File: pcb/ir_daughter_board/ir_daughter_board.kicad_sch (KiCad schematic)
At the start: 5 parts, among them J1 USB_OTG

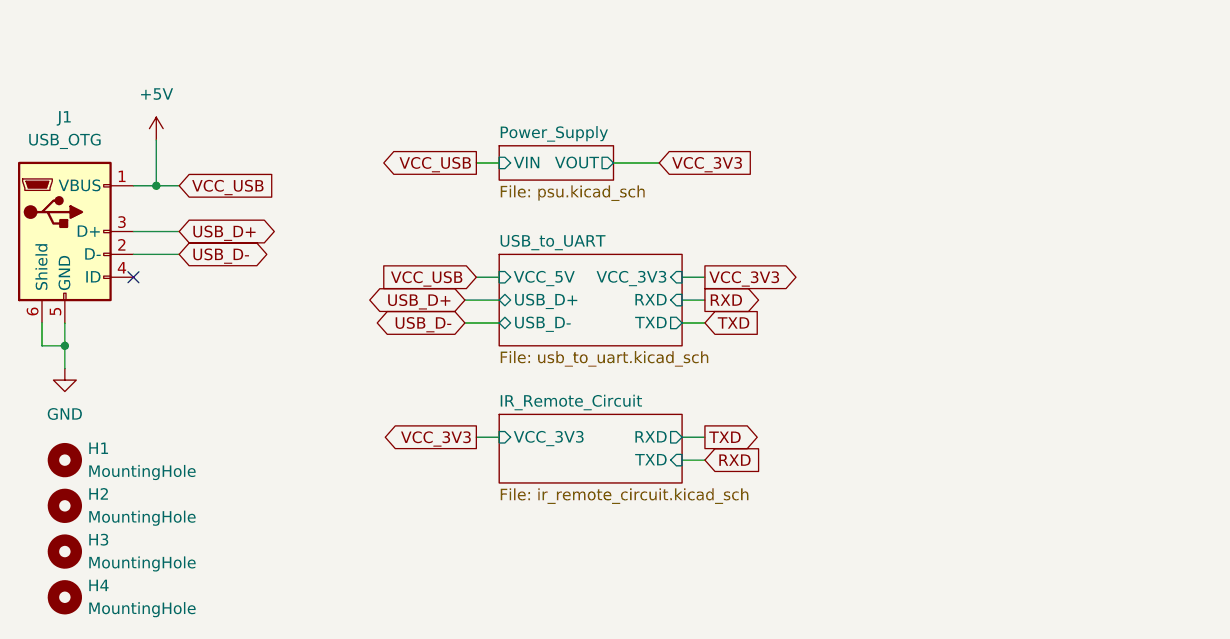
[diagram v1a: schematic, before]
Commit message: refined circuit with reddit comments
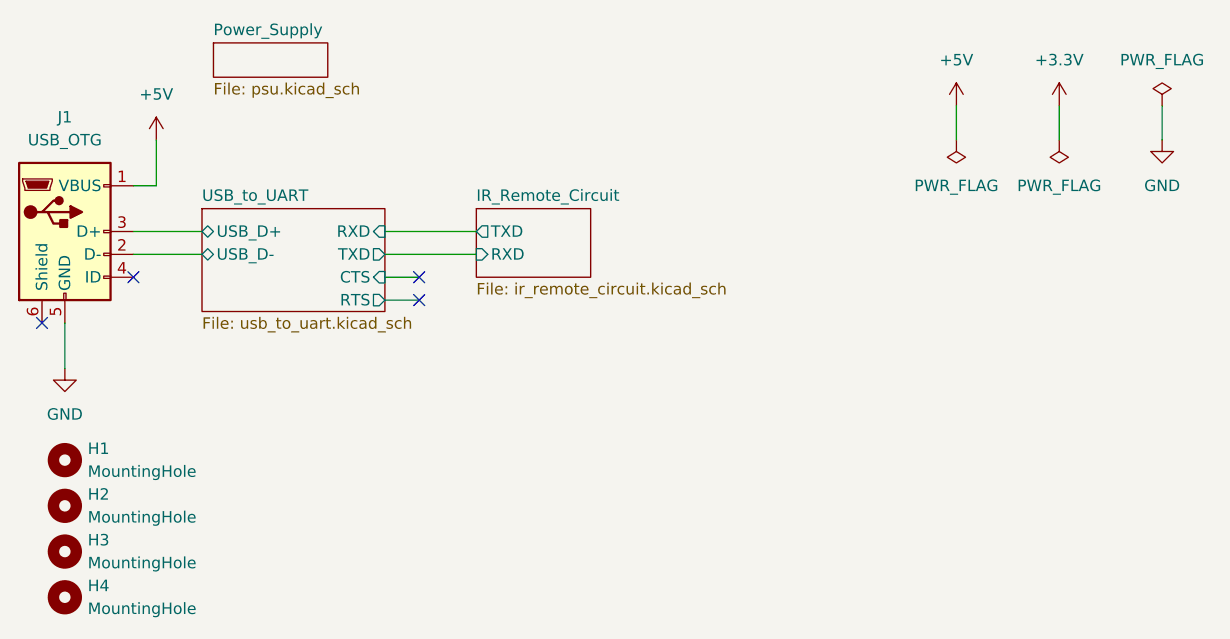
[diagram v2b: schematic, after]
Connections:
- net GND: no longer J1.6 (Shield)
- net USB_D+ renamed USB_to_UART/USB_D+
- net USB_D- renamed USB_to_UART/USB_D-
- no-connect marks 1 -> 4
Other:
- sheet IR_Remote_Circuit ports: added none; removed VCC_3V3
- sheet Power_Supply ports: added none; removed VIN, VOUT
- sheet USB_to_UART ports: added CTS, RTS; removed VCC_3V3, VCC_5V
